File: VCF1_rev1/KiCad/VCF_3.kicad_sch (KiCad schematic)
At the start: 13 parts, among them U10 Opamp_Quad, U3 CEM3350, U9 LM13700

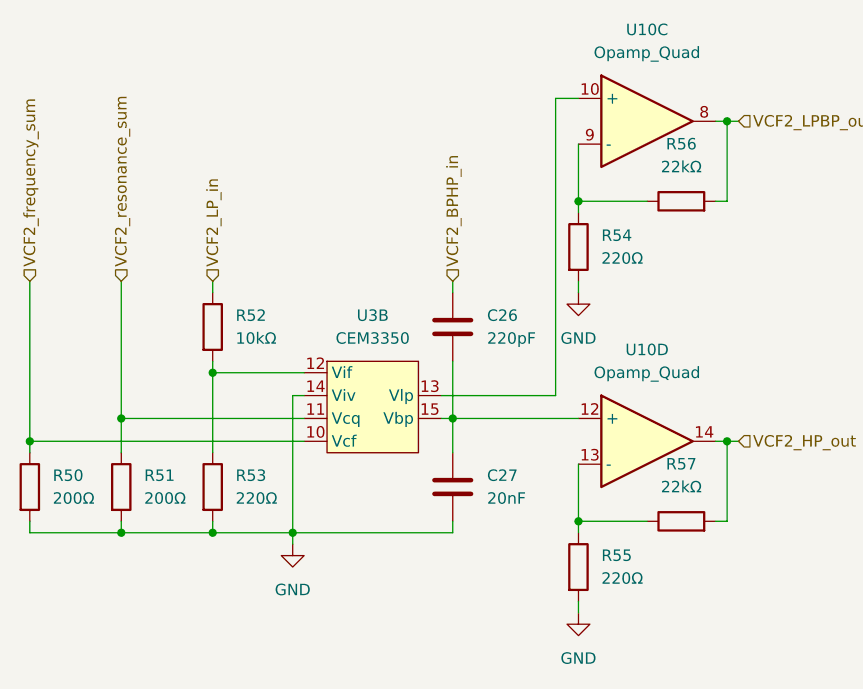
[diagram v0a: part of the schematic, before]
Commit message: Added VCA (with a quirk) and also drew a new symbol for 74HC4053 because the standard one annoyed me.
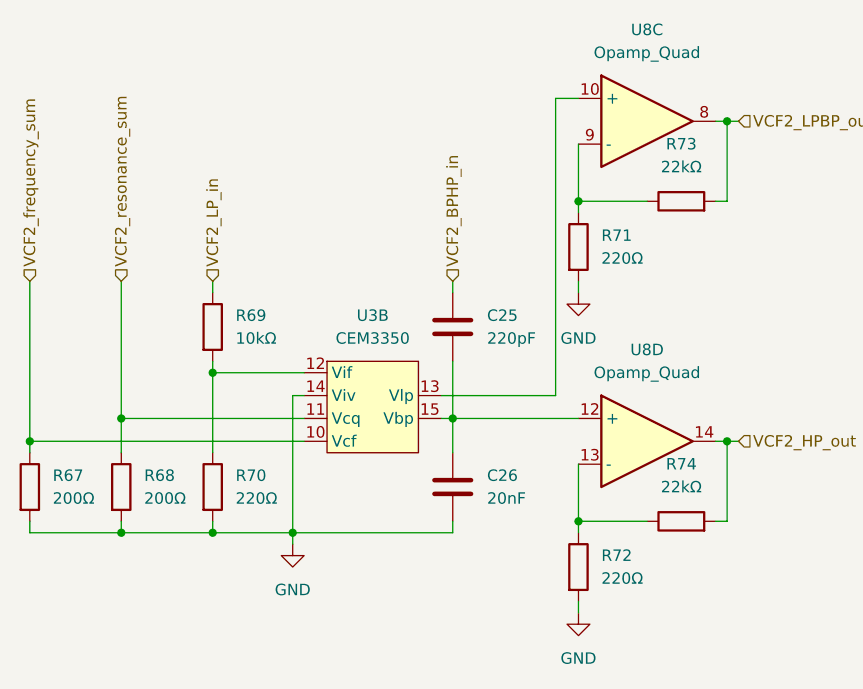
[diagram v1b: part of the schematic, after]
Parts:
- renumbered C26 to C25, C27 to C26, R50 to R67, R51 to R68, R52 to R69, R53 to R70, R54 to R71, R55 to R72, R56 to R73, R57 to R74, U10 to U8

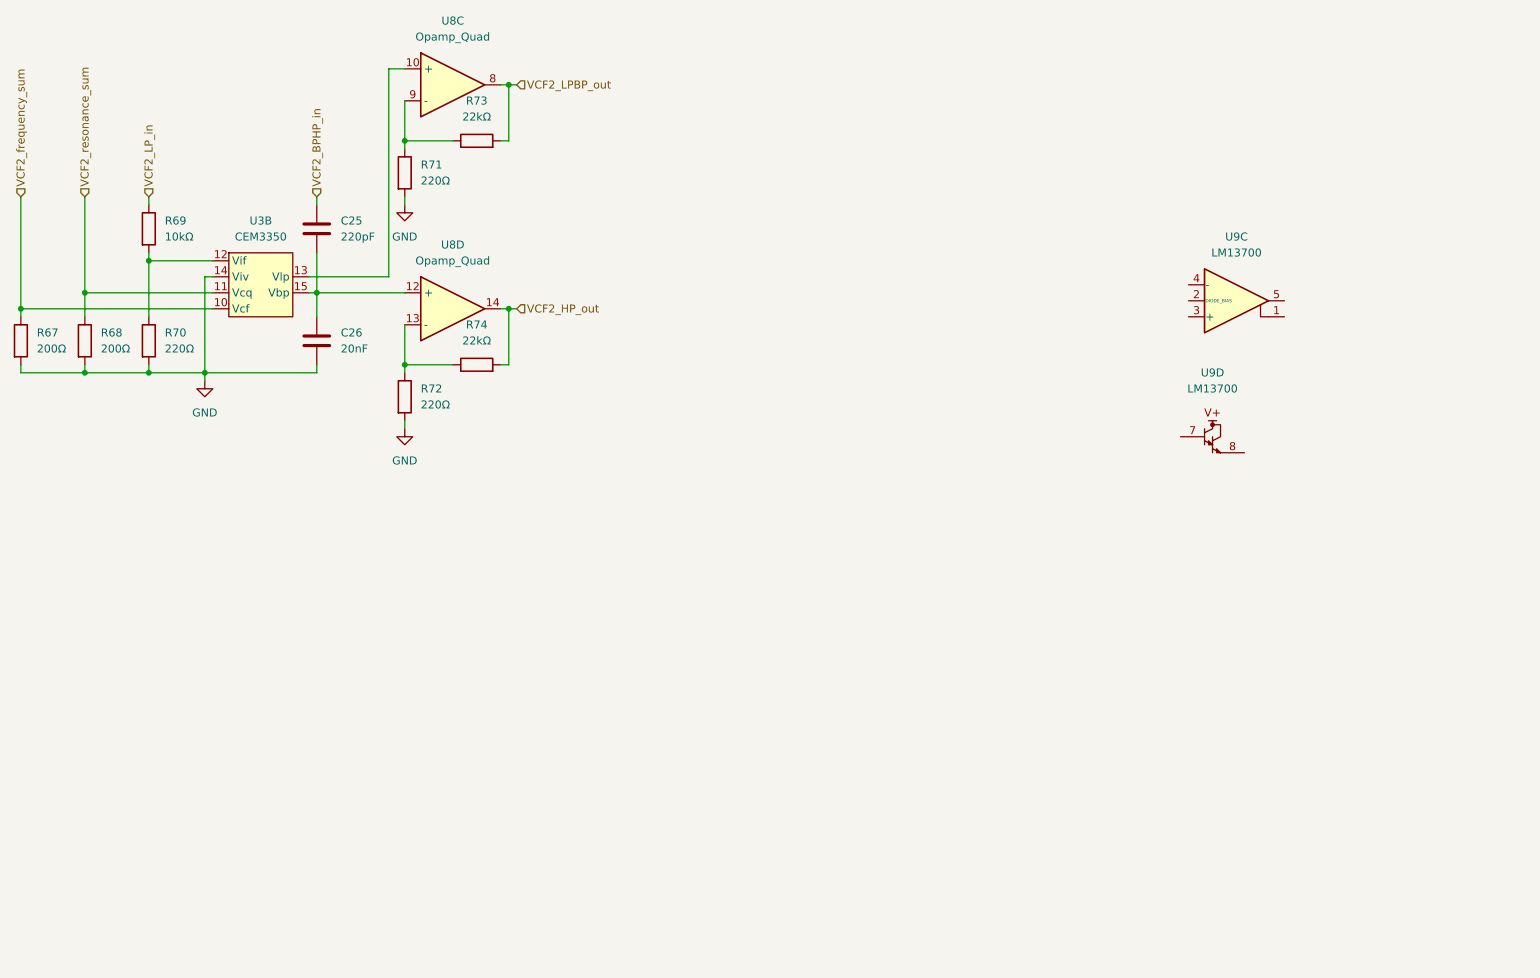
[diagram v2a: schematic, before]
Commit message: The filter blocks are more or less done, page order has gotten more sane for easier reading.
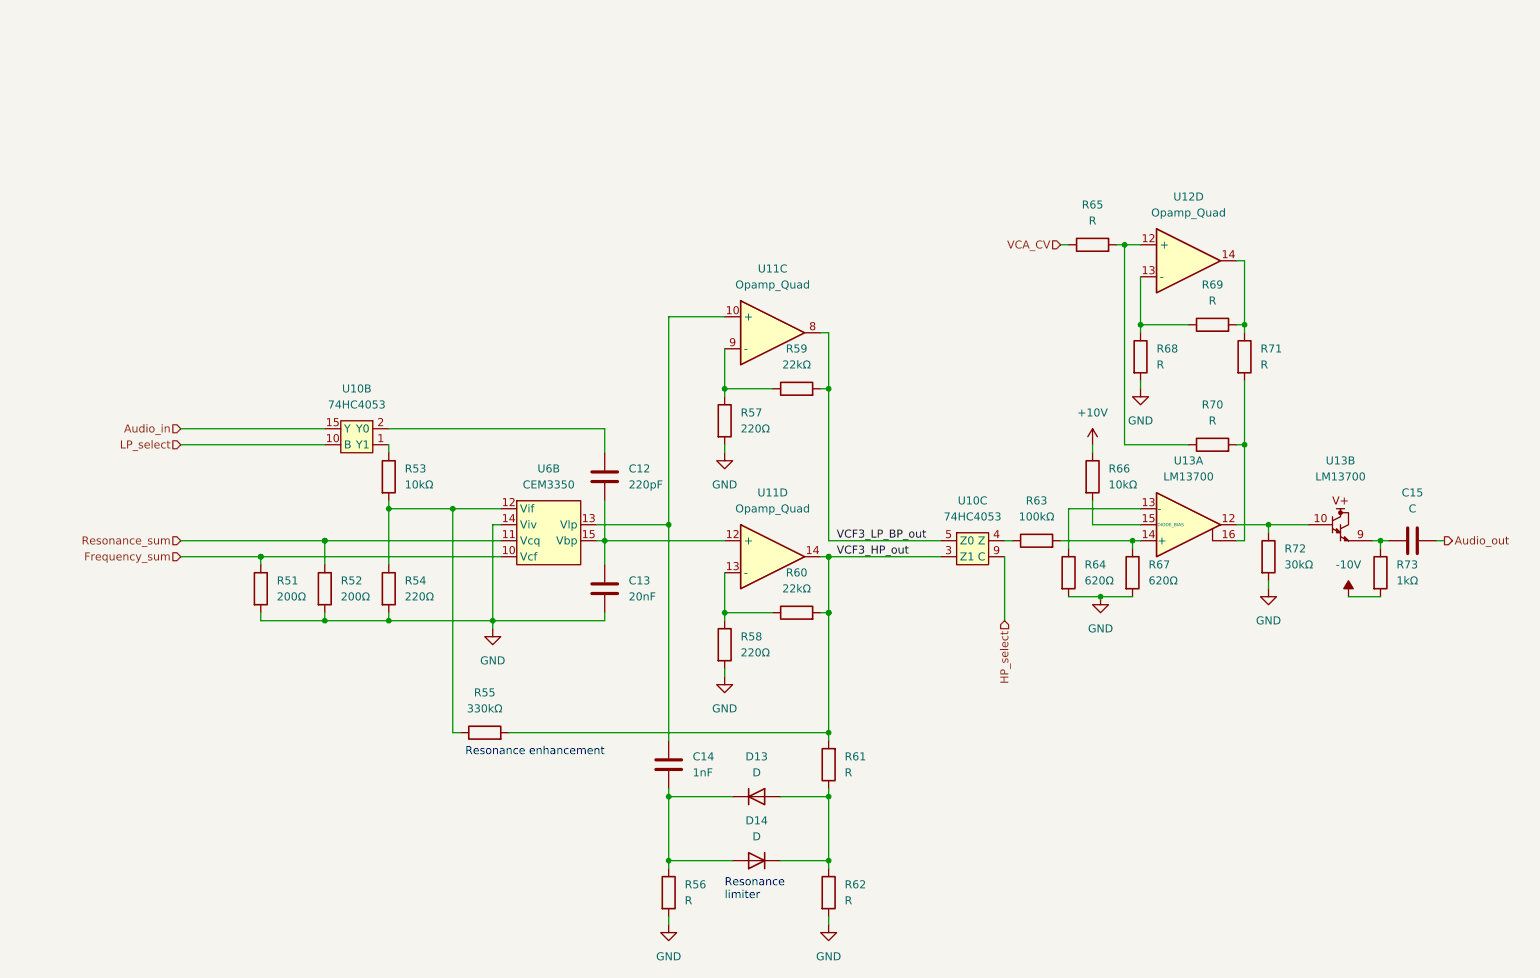
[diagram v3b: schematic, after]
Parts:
- removed U9: LM13700, symbol Amplifier_Operational:LM13700
- added C14: 1nF, symbol Device:C
- added C15: C, symbol Device:C
- added D13, D14: D, symbol Device:D
- added R55: 330kΩ, symbol Device:R
- added R56, R61, R62, R65, R68, R69, R70, R71: R, symbol Device:R
- added R63: 100kΩ, symbol Device:R
- added R64, R67: 620Ω, symbol Device:R
- added R66: 10kΩ, symbol Device:R
- added R72: 30kΩ, symbol Device:R
- added R73: 1kΩ, symbol Device:R
- added U10: 74HC4053, symbol Modular_Mayhem:74HC4053
- added U12: Opamp_Quad, symbol Device:Opamp_Quad
- added U13: LM13700, symbol Amplifier_Operational:LM13700
- renumbered C25 to C12, C26 to C13, R67 to R51, R68 to R52, R69 to R53, R70 to R54, R71 to R57, R72 to R58, R73 to R59, R74 to R60, U8 to U11, U3 to U6
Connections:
- net GND: now also R56.2, R62.2, R64.2, R67.2, R68.2, R72.2
- net at U11.10 (+), U6.13 (Vlp): now also C14.2
- net at R53.2, R54.1, U6.12 (Vif): now also R55.1
- net VCF2_BPHP_in: no longer names the net of C12.1
- net VCF2_BPHP_in: now also U10.2 (Y0)
- net VCF2_HP_out: no longer names the net of R60.2, U11.14
- net VCF2_HP_out: now also R55.2, R61.2
- net VCF2_LPBP_out renamed VCF3_LP_BP_out
- net VCF3_LP_BP_out: now also U10.5 (Z0)
- net VCF2_LP_in: no longer names the net of R53.1
- net VCF2_LP_in: now also U10.1 (Y1)
- net VCF2_frequency_sum renamed Frequency_sum
- net VCF2_resonance_sum renamed Resonance_sum
- new net: R68.1, R69.1, U12.13 (-)
- new net: C14.1, D13.1 (K), D14.2 (A), R56.1
- new net: R64.1, U13.13 (-)
- new net: D13.2 (A), D14.1 (K), R61.1, R62.1
- new net: R66.2, U13.15 (DIODE_BIAS)
- new net: R72.1, U13.10, U13.12
- new net: C15.1, R73.1, U13.9
- new net: R69.2, R71.1, U12.14
- new net: R63.2, R67.1, U13.14 (+)
- new net: R65.2, R70.1, U12.12 (+)
- new net: R70.2, R71.2, U13.16
- new net: R63.1, U10.4 (Z)
- new net +10V: R66.1
- new net -10V: R73.2
- new net Audio_in: U10.15 (Y)
- new net Audio_out: C15.2
- new net HP_select: U10.9 (C)
- new net LP_select: U10.10 (B)
- new net VCA_CV: R65.1
- new net VCF3_HP_out: U10.3 (Z1)
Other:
- note added: "Resonance enhancement"
- note added: "Resonance limiter"
- moved on the sheet: C12, C13, R51, R52, R53, R54, R57, R58, R59, R60, U11C, U11D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

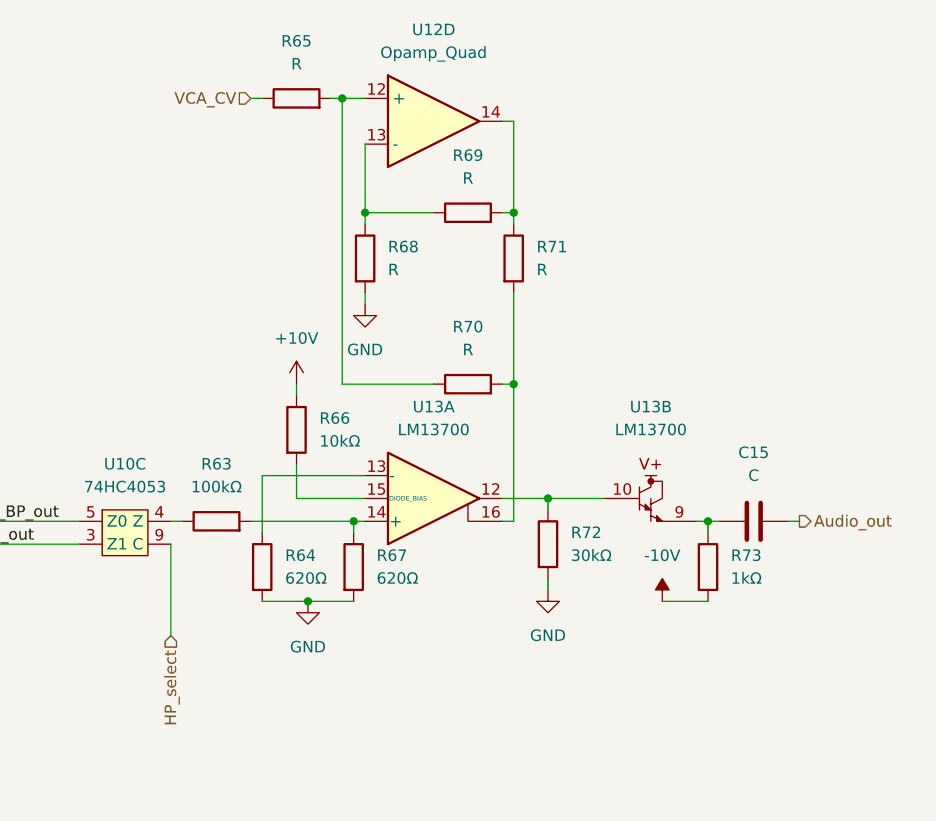
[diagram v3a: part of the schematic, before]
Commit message: Added the MUX. The signal path is now more or less complete!
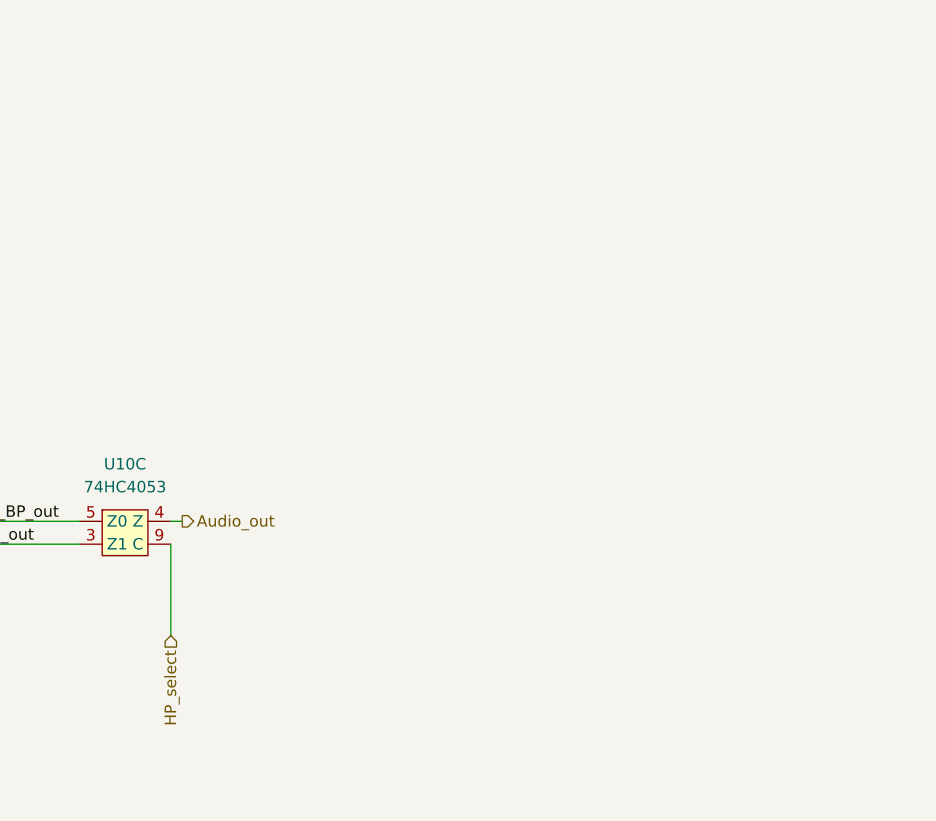
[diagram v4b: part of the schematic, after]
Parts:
- removed C15: C, symbol Device:C
- removed R63: 100kΩ, symbol Device:R
- removed R64, R67: 620Ω, symbol Device:R
- removed R65, R68, R69, R70, R71: R, symbol Device:R
- removed R66: 10kΩ, symbol Device:R
- removed R72: 30kΩ, symbol Device:R
- removed R73: 1kΩ, symbol Device:R
- removed U12: Opamp_Quad, symbol Device:Opamp_Quad
- removed U13: LM13700, symbol Amplifier_Operational:LM13700
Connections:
- net Audio_out: now also U10.4 (Z)

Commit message: Lot of work on panel etc.
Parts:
- renumbered R51 to R72, R52 to R73, R53 to R74, R54 to R75, R55 to R76, R56 to R77, R57 to R78, R58 to R79, R59 to R80, R60 to R81, R61 to R82, R62 to R83, U6 to U10, U10 to U13, U11 to U14
